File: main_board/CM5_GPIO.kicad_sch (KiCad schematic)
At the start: 7 parts, among them SW1 Right angle Tact button, U5 74LVC1G07SE-7

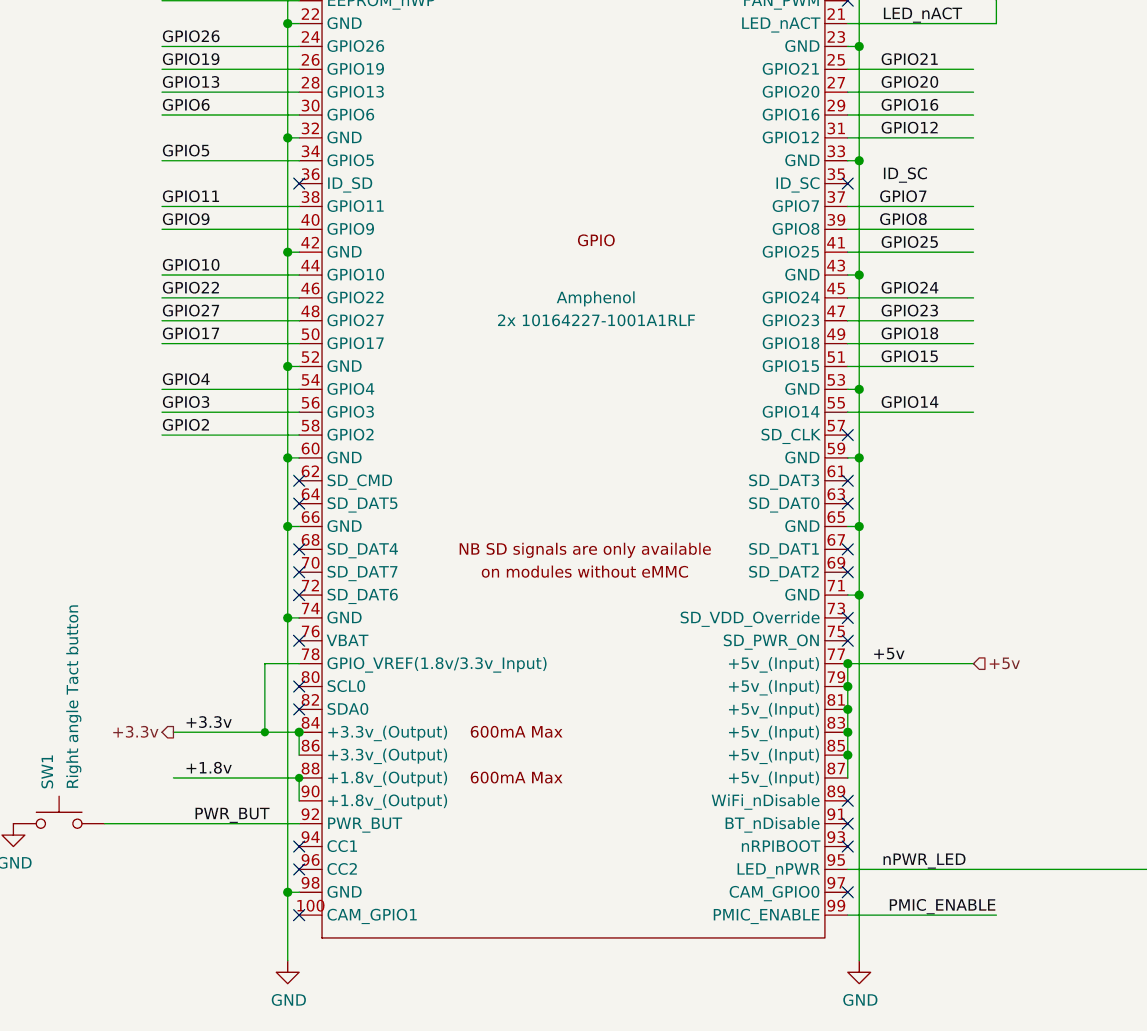
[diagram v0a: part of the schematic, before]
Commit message: Implement part of power management.
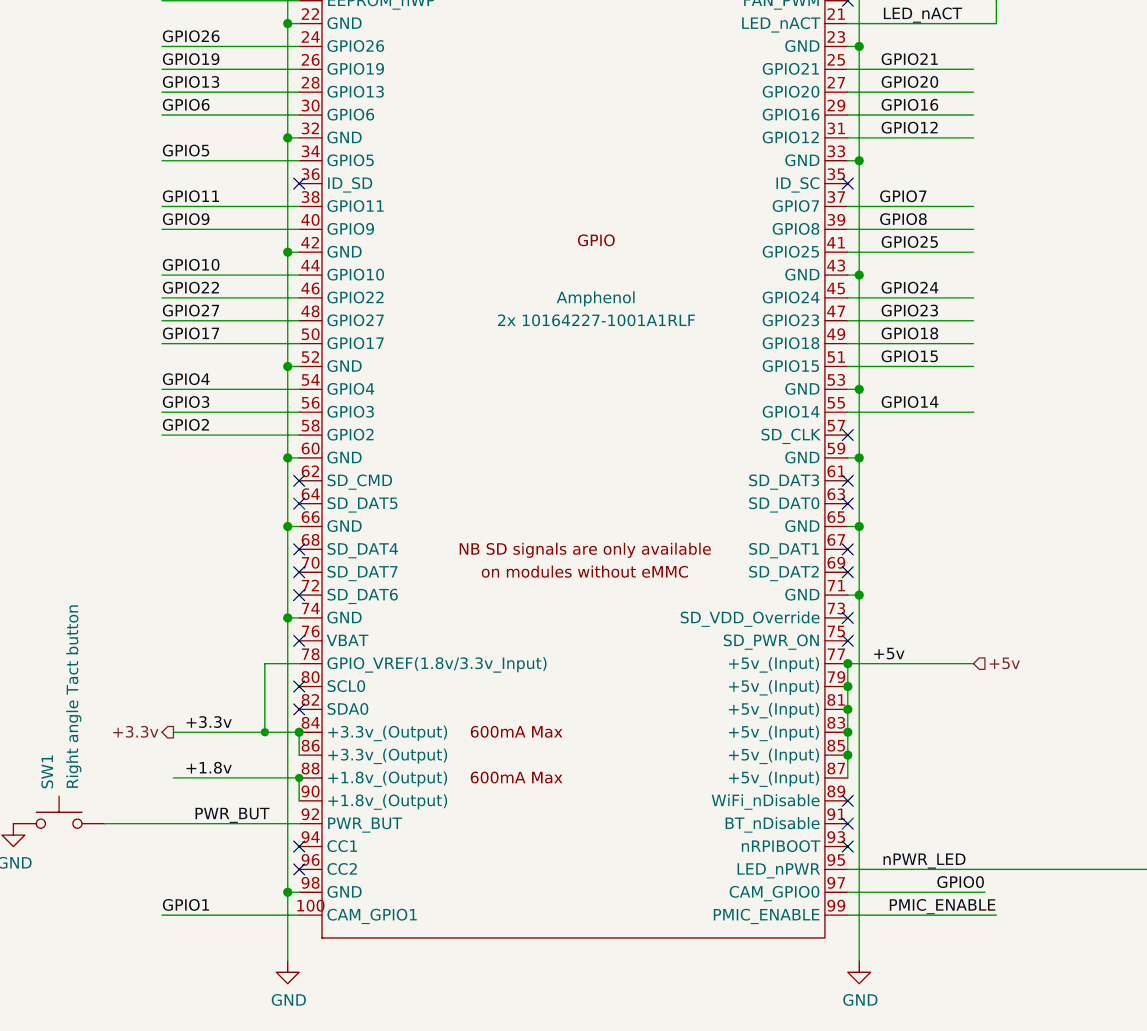
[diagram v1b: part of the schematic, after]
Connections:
- net GPIO1: now reaches Module1.100 (CAM_GPIO1)
- net GPIO0: now reaches Module1.97 (CAM_GPIO0)
- no-connect marks 37 -> 35
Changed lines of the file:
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@@
-	)
-	(no_connect
-		(at 83.82 147.32)
 	)
 	(no_connect
@@
 	)
 	(no_connect
-		(at 144.78 144.78)
-	)
-	(no_connect
 		(at 144.78 109.22)
 	)
@@
 	(wire
 		(pts
+			(xy 160.02 144.78) (xy 144.78 144.78)
+		)
+		(stroke
+			(width 0)
+			(type solid)
+		)
+	)
+	(wire
+		(pts
 			(xy 214.63 125.73) (xy 214.63 128.27)
 		)
@@
 		(pts
 			(xy 144.78 86.36) (xy 158.75 86.36)
+		)
+		(stroke
+			(width 0)
+			(type solid)
+		)
+	)
+	(wire
+		(pts
+			(xy 68.58 147.32) (xy 83.82 147.32)
 		)
 		(stroke
@@
 		)
 	)
+	(label "GPIO0"
+		(at 160.02 144.78 180)
+		(fields_autoplaced yes)
+		(effects
+			(font
+				(size 1.27 1.27)
+			)
+			(justify right bottom)
+		)
+	)
 	(label "LED_nACT"
 		(at 157.48 48.26 180)
@@
 		)
 	)
-	(label "ID_SC"
-		(at 153.67 66.04 180)
-		(fields_autoplaced yes)
-		(effects
-			(font
-				(size 1.27 1.27)
-			)
-			(justify right bottom)
-		)
-	)
 	(label "+5v"
 		(at 151.13 119.38 180)
@@
 		(fields_autoplaced yes)
 		(effects
+			(font
+				(size 1.27 1.27)
+			)
+			(justify left bottom)
+		)
+	)
+	(label "GPIO1"
+		(at 68.58 147.32 0)
+		(fields_autoplaced yes)
+		(effects

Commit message: More power management goodness
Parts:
- removed SW1: Right angle Tact button, Button_Switch_SMD:SW_Push_1P1T_NO_CK_KSC7xxJ, symbol Switch:SW_Push
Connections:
- net +5v renamed +5V
- net GPIO0 renamed CM5_SCL
- net GPIO1 renamed CM5_SDA
- net PMIC_ENABLE renamed CM5_PMIC_EN
- no-connect marks 35 -> 62

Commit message: Finalize power management
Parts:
- removed D1: LED Red, LED_SMD:LED_0805_2012Metric_Pad1.15x1.40mm_HandSolder, symbol Device:LED
- removed D2: LED Green, LED_SMD:LED_0805_2012Metric_Pad1.15x1.40mm_HandSolder, symbol Device:LED
- removed R1, R10: 1k, Resistor_SMD:R_0805_2012Metric_Pad1.20x1.40mm_HandSolder, symbol Device:R
- removed U5: 74LVC1G07SE-7, Package_TO_SOT_SMD:SOT-353_SC-70-5, symbol CM5IO:74LVC1G07_copy
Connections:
- net LED_nACT: no longer names the net of Module1.21 (LED_nACT)
- net nPWR_LED: no longer names the net of Module1.95 (LED_nPWR)
- no-connect marks 62 -> 64
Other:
- note removed: "Activity LED"
- note removed: "PWR LED"

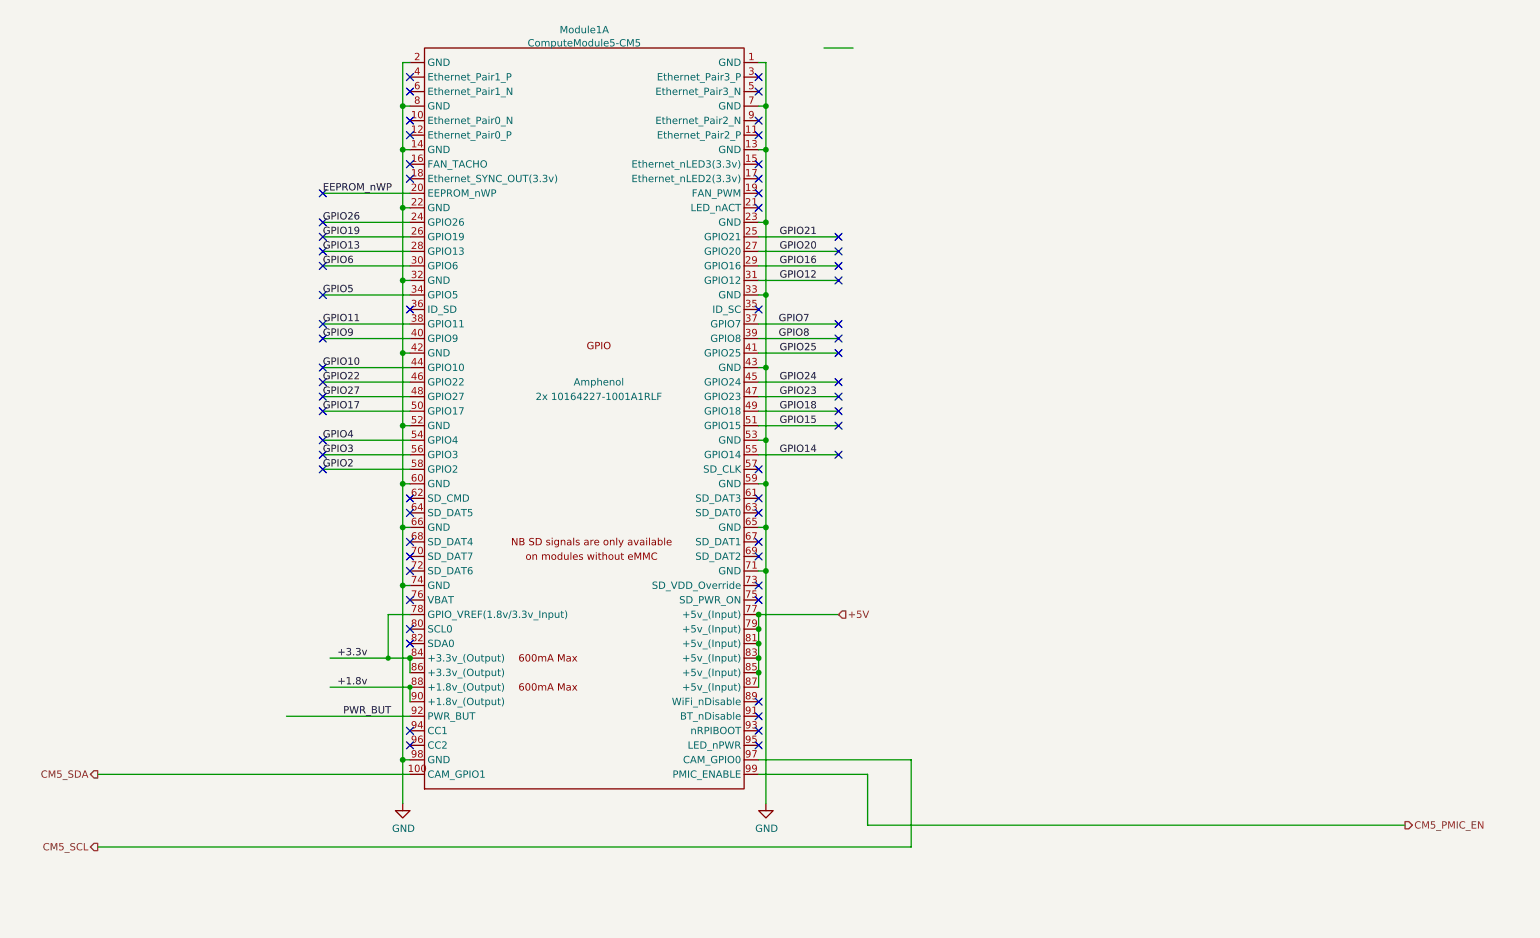
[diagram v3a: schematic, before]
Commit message: Bunch more routing, mainly added MIPI interface, reworked power management a bit
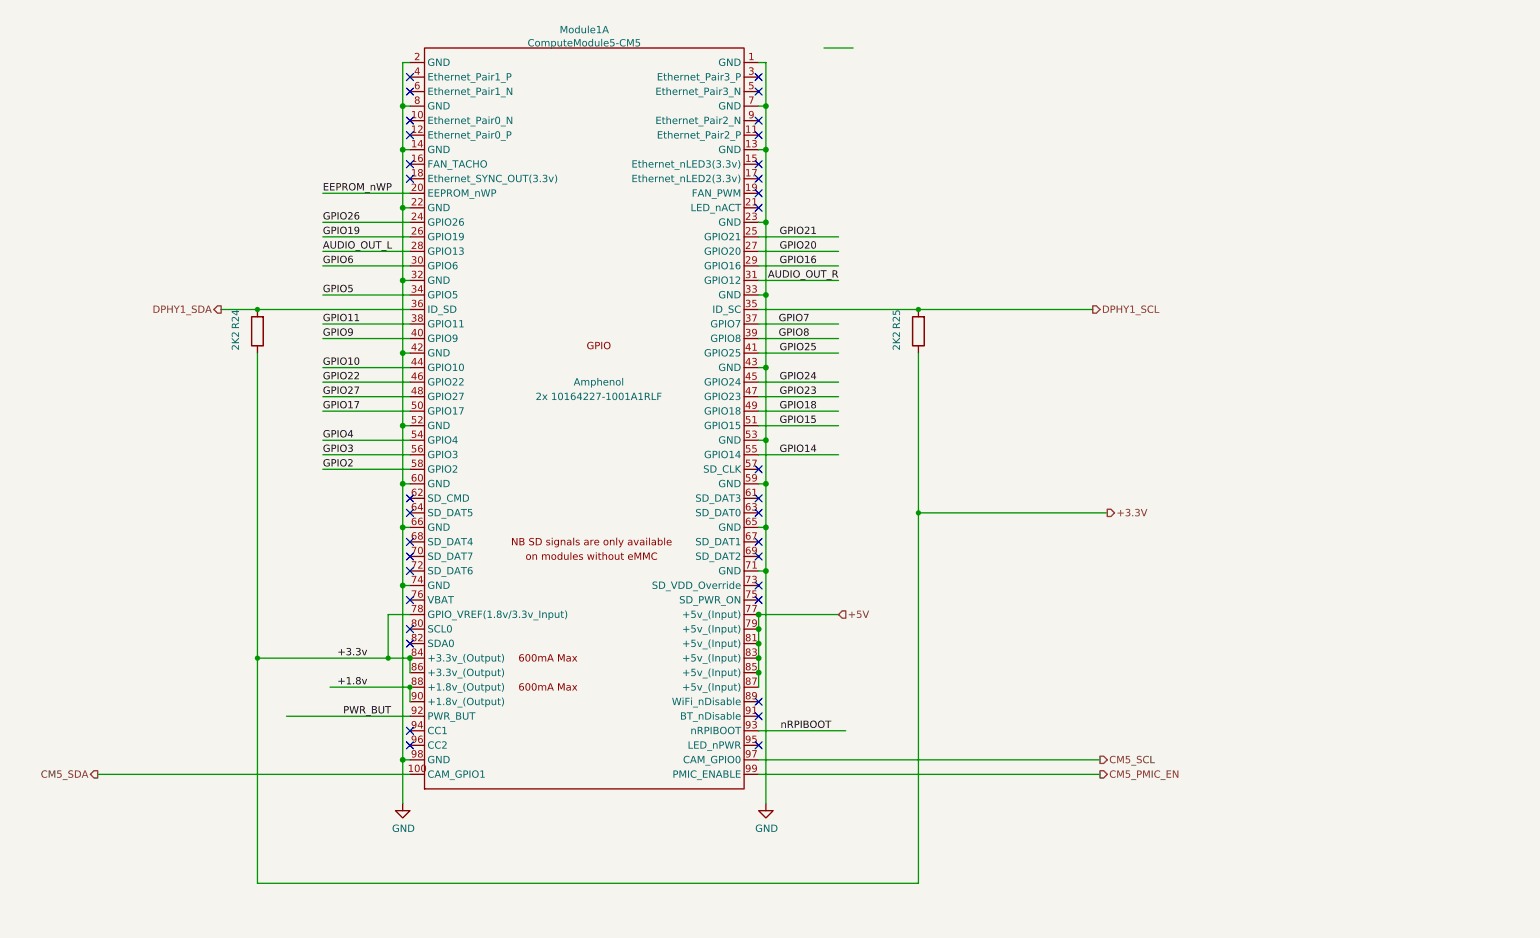
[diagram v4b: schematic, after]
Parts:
- added R24, R25: 2K2, Resistor_SMD:R_0805_2012Metric_Pad1.20x1.40mm_HandSolder, symbol Device:R
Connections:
- net DPHY1_SCL: now reaches Module1.35 (ID_SC)
- net DPHY1_SCL: now also R25.2
- net DPHY1_SDA: now reaches Module1.36 (ID_SD)
- net DPHY1_SDA: now also R24.2
- net nRPIBOOT: now reaches Module1.93 (nRPIBOOT)
- net +3.3v renamed +3.3V
- net +3.3V: now also R24.1, R25.1
- net GPIO12 renamed AUDIO_OUT_R
- net GPIO13 renamed AUDIO_OUT_L
- no-connect marks 64 -> 34

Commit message: Bunch of fixes + audio out interface
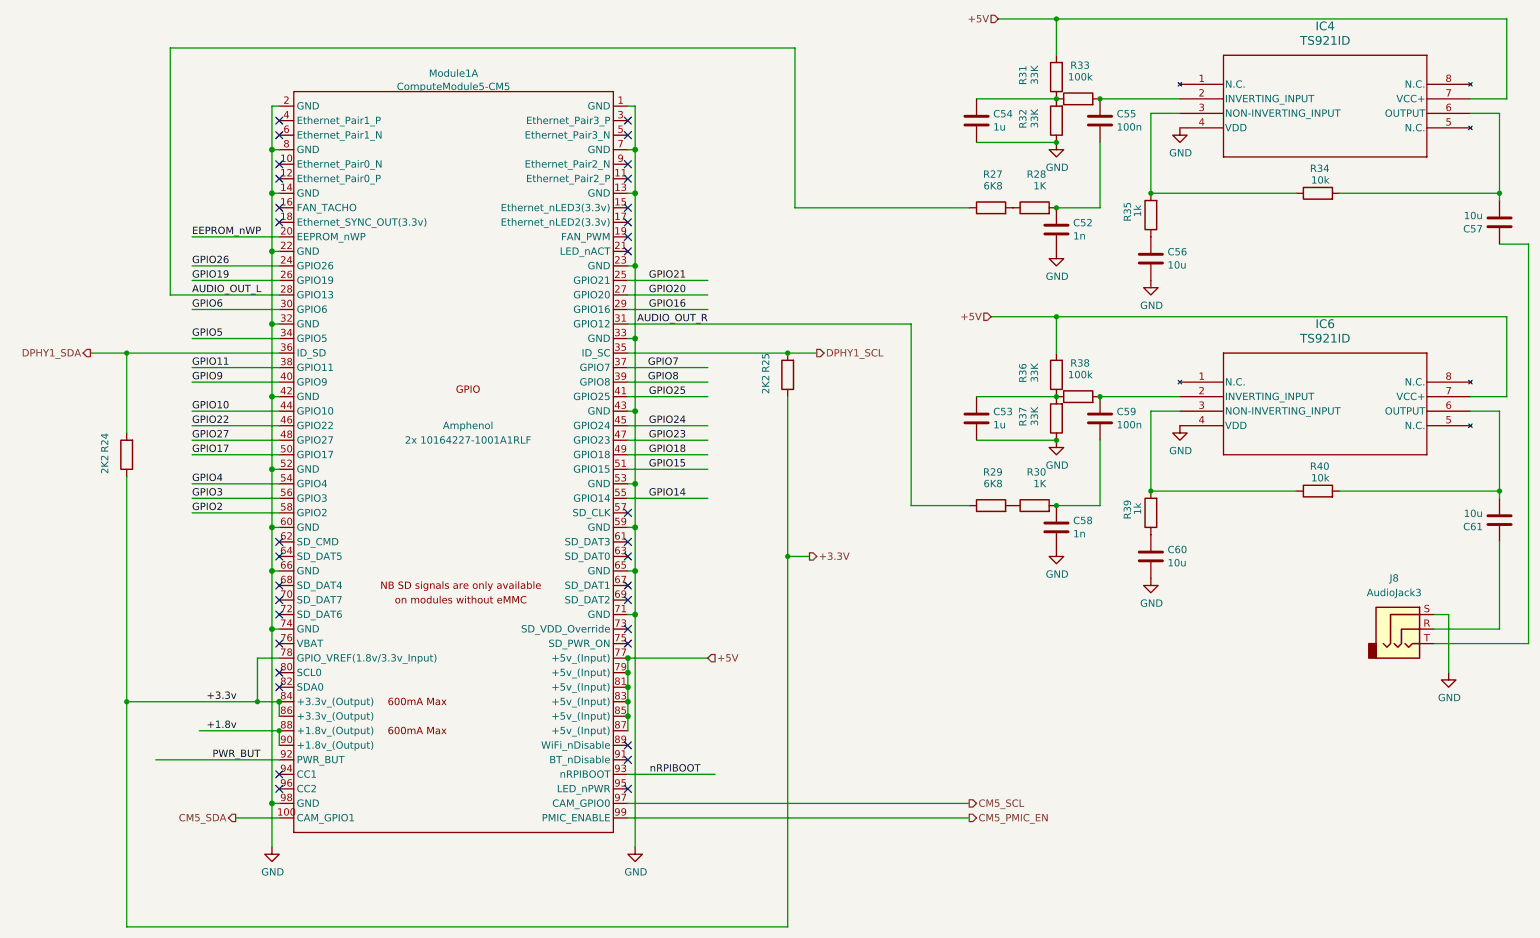
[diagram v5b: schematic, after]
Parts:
- added C52, C58: 1n, Capacitor_SMD:C_0805_2012Metric_Pad1.18x1.45mm_HandSolder, symbol Device:C
- added C53, C54: 1u, Capacitor_SMD:C_0805_2012Metric_Pad1.18x1.45mm_HandSolder, symbol Device:C
- added C55, C59: 100n, Capacitor_SMD:C_0805_2012Metric_Pad1.18x1.45mm_HandSolder, symbol Device:C
- added C56, C57, C60, C61: 10u, Capacitor_SMD:C_0805_2012Metric_Pad1.18x1.45mm_HandSolder, symbol Device:C
- added IC4, IC6: TS921ID, 000_custom:S0-8_3P9X4P9_STM, symbol 000_Custom:TS921ID
- added J8: AudioJack3, Connector_Audio:Jack_3.5mm_CUI_SJ1-3523N_Horizontal, symbol Connector_Audio:AudioJack3
- added R27, R29: 6K8, Resistor_SMD:R_0805_2012Metric_Pad1.20x1.40mm_HandSolder, symbol Device:R
- added R28, R30: 1K, Resistor_SMD:R_0805_2012Metric_Pad1.20x1.40mm_HandSolder, symbol Device:R
- added R31, R32, R36, R37: 33K, Resistor_SMD:R_0805_2012Metric_Pad1.20x1.40mm_HandSolder, symbol Device:R
- added R33, R38: 100k, Resistor_SMD:R_0805_2012Metric_Pad1.20x1.40mm_HandSolder, symbol Device:R
- added R34, R40: 10k, Resistor_SMD:R_0805_2012Metric_Pad1.20x1.40mm_HandSolder, symbol Device:R
- added R35, R39: 1k, Resistor_SMD:R_0805_2012Metric_Pad1.20x1.40mm_HandSolder, symbol Device:R
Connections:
- net +5V: now also IC4.7 (VCC+), IC6.7 (VCC+), R31.2, R36.2
- net AUDIO_OUT_L: now also R27.1
- net AUDIO_OUT_R: now also R29.1
- net GND: now also C52.2, C53.2, C54.2, C56.2, C58.2, C60.2, IC4.4 (VDD), IC6.4 (VDD), J8.S, R32.1, R37.1
- new net: C53.1, R36.1, R37.2, R38.1
- new net: IC4.3 (NON-INVERTING_INPUT), R34.1, R35.2
- new net: C57.2, IC4.6 (OUTPUT), R34.2
- new net: C60.1, R39.1
- new net: IC6.3 (NON-INVERTING_INPUT), R39.2, R40.1
- new net: C61.1, J8.R
- new net: C61.2, IC6.6 (OUTPUT), R40.2
- new net: C54.1, R31.1, R32.2, R33.1
- new net: C52.1, C55.2, R28.2
- new net: C56.1, R35.1
- new net: R27.2, R28.1
- new net: C55.1, IC4.2 (INVERTING_INPUT), R33.2
- new net: C57.1, J8.T
- new net: C59.1, IC6.2 (INVERTING_INPUT), R38.2
- new net: C58.1, C59.2, R30.2
- new net: R29.2, R30.1
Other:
- moved on the sheet: Module1A, R24, R25

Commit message: Implement power monitoring
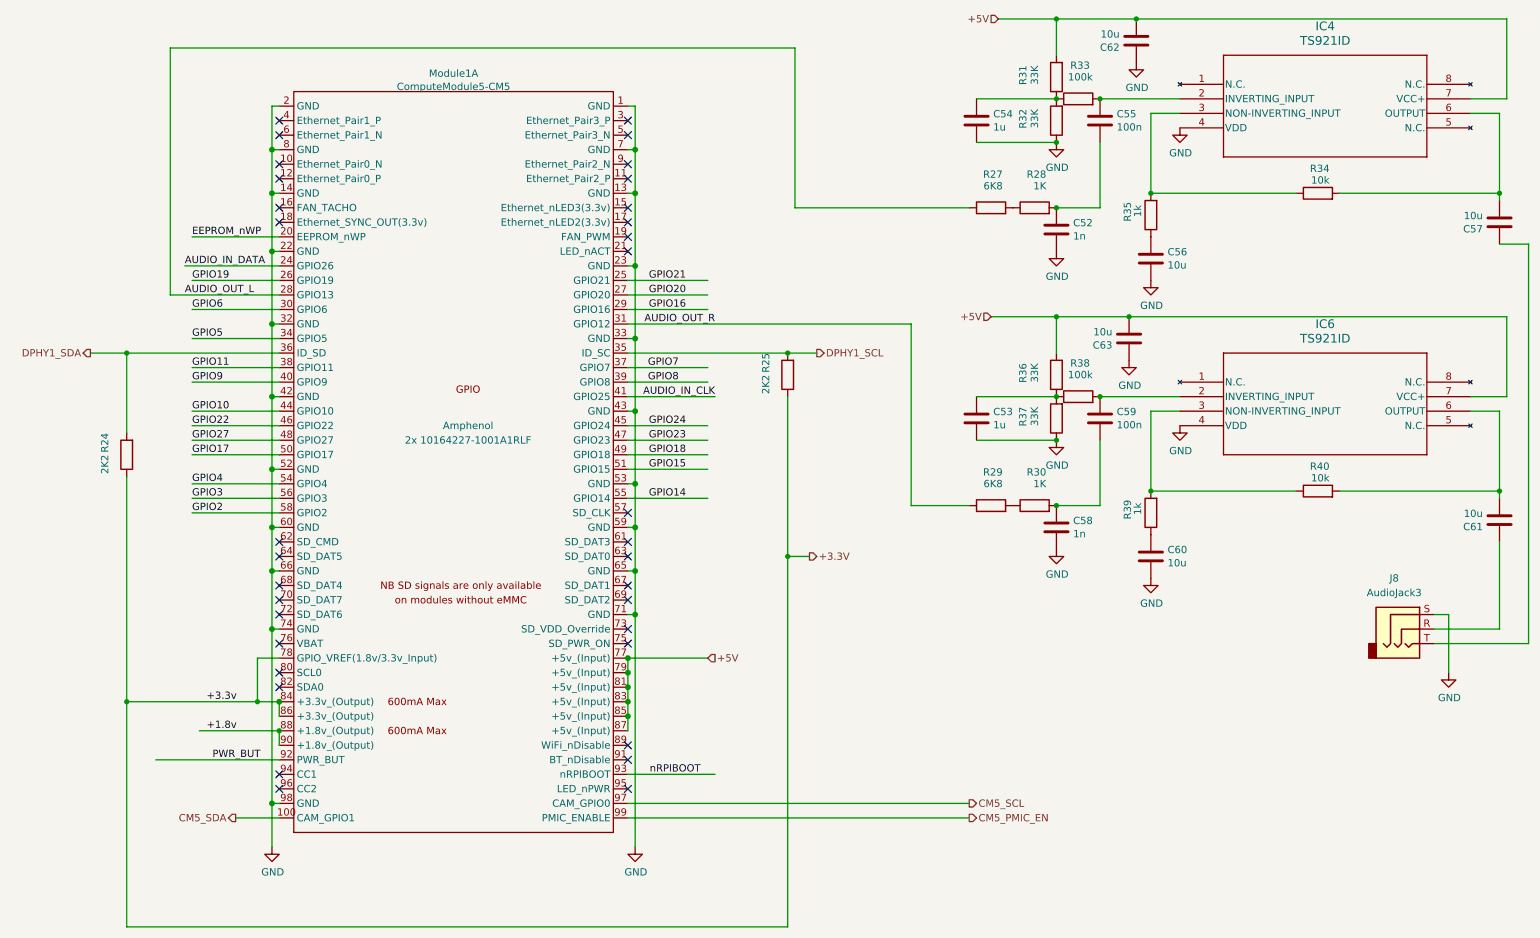
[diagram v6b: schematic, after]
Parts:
- added C62, C63: 10u, Capacitor_SMD:C_0805_2012Metric_Pad1.18x1.45mm_HandSolder, symbol Device:C
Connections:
- net +5V: now also C62.2, C63.2
- net GND: now also C62.1, C63.1
- net GPIO25 renamed AUDIO_IN_CLK
- net GPIO26 renamed AUDIO_IN_DATA
